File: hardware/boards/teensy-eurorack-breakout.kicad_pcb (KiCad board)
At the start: 4 copper layers, 110.5 x 111.1 mm, 76 parts, among them J1 Conn_01x08, SW1 Rotary_Encoder_Switch, SW2 Rotary_Encoder_Switch, SW3 Rotary_Encoder_Switch, U2 AD5754BREZ, U3 AD5754BREZ, U5 MCP1700-2502E, U6 AD7606BSTZ, U7 6N138

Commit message: schematic, pcb changes for v2.0
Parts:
- removed R2: 4.7k, Resistor_SMD:R_0805_2012Metric
- C19, C21, C23, C25, C31, C32, C33, C34: footprint Capacitor_SMD:C_0805_2012Metric -> Capacitors_THT:CP_Radial_D5.0mm_P2.00mm
- moved C19 41.8 mm to (105.4, 113.7), turned to 0 degrees
- moved C23 40.3 mm to (105.4, 107.3), turned to 0 degrees
- moved C32 40.2 mm to (99.1, 107.3), turned to 0 degrees
- moved U5 35.8 mm to (126.9, 123.3)
- moved C33 33.5 mm to (99.1, 113.7), turned to 0 degrees
- moved C30 31.2 mm to (120.0, 102.9)
- moved C27 30.7 mm to (126.9, 131.2), turned to 0 degrees
- moved C28 30.7 mm to (126.9, 127.5), turned to 0 degrees
- moved U3 29.7 mm to (118.1, 96.5), turned to 270 degrees
- moved C29 25.9 mm to (115.9, 102.9), turned to 180 degrees
- moved C37 25.3 mm to (109.5, 102.9), turned to 0 degrees
- moved C39 24.5 mm to (105.7, 102.9)
- moved C34 20.5 mm to (120.0, 113.7), turned to 0 degrees
- moved C35 17.0 mm to (142.2, 114.9), turned to 270 degrees
- moved C31 16.6 mm to (120.0, 107.3), turned to 0 degrees
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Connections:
- JB1 pad 13: +12V -> -12V
- JB1 pad 14: -12V -> +12V
- JB1 pad 5: Net-(JB1-Pad5) -> GND
- JB1 pad 6: Net-(JB1-Pad6) -> /ADC_RESET
- JB1 pad 7: Net-(JB1-Pad7) -> GND
- JB2 pad 13: +12V -> (no net)
- JB2 pad 14: -12V -> (no net)
- JB2 pad 3: /ADC_SCK -> /ADC_RANGE
- JB2 pad 7: /DAC_SDOUT -> GND
- JOUT1 pad TN: Net-(JOUT1-PadTN) -> (no net)
- JOUT2 pad TN: Net-(JOUT2-PadTN) -> (no net)
- JOUT3 pad TN: Net-(JOUT3-PadTN) -> (no net)
- JOUT4 pad TN: Net-(JOUT4-PadTN) -> (no net)
- JOUT5 pad TN: Net-(JOUT5-PadTN) -> (no net)
- JOUT6 pad TN: Net-(JOUT6-PadTN) -> (no net)
- JOUT7 pad TN: Net-(JOUT7-PadTN) -> (no net)
- JOUT8 pad TN: Net-(JOUT8-PadTN) -> (no net)
- MIDI_IN1 pad 1: Net-(MIDI_IN1-Pad1) -> (no net)
- MIDI_IN1 pad 3: Net-(MIDI_IN1-Pad3) -> (no net)
- MIDI_IN1 pad 5: Net-(MIDI_IN1-Pad5) -> (no net)
- MIDI_OUT1 pad 1: Net-(MIDI_OUT1-Pad1) -> (no net)
- MIDI_OUT1 pad 3: Net-(MIDI_OUT1-Pad3) -> (no net)
- MIDI_OUT1 pad 5: Net-(MIDI_OUT1-Pad5) -> (no net)
- R1 pad 2: Net-(R1-Pad2) -> /ADC_RESET
- U2 pad 12: Net-(U2-Pad12) -> (no net)
- U2 pad 13: Net-(U2-Pad13) -> (no net)
- U2 pad 2: Net-(U2-Pad2) -> (no net)
- U2 pad 6: Net-(U2-Pad6) -> (no net)
- U3 pad 12: Net-(U3-Pad12) -> (no net)
- U3 pad 13: Net-(U3-Pad13) -> (no net)
- U3 pad 16: /DAC_SDOUT -> (no net)
- U3 pad 2: Net-(U3-Pad2) -> (no net)
- U3 pad 6: Net-(U3-Pad6) -> (no net)
- U6 pad 11: Net-(R1-Pad2) -> /ADC_RESET
- U6 pad 12: /ADC_SCK -> /DAC_SCK
- U6 pad 15: Net-(U6-Pad15) -> (no net)
- U6 pad 42: Net-(U6-Pad42) -> (no net)
- U6 pad 8: Net-(R2-Pad1) -> /ADC_RANGE
- U7 pad 1: Net-(U7-Pad1) -> (no net)
- U7 pad 4: Net-(U7-Pad4) -> (no net)
- U7 pad 7: Net-(U7-Pad7) -> (no net)
- USBA1 pad 5: Net-(USBA1-Pad5) -> (no net)
- USBA1 pad 6: Net-(USBA1-Pad6) -> (no net)
- USBB1 pad 5: Net-(USBB1-Pad5) -> (no net)
- USBB1 pad 6: Net-(USBB1-Pad6) -> (no net)
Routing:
- net GND: track 97.8 -> 817.8 mm, vias 22 -> 239
- net /VOUT5: track 42.6 -> 197.7 mm
- net +5V: track 198.0 -> 315.4 mm, vias 0 -> 5
- net /ADC_RESET: track 0.00 -> 75.3 mm
- net /VOUT7: track 46.6 -> 115.2 mm
- net +12V: track 129.5 -> 61.5 mm, vias 2 -> 1
- net /DAC_SDOUT: track 59.7 -> 0.00 mm, vias 1 -> 0
- net /ADC_RANGE: track 0.00 -> 57.1 mm
- net /ADC_SCK: track 56.7 -> 0.00 mm, vias 1 -> 0
- net /VOUT8: track 51.3 -> 105.1 mm, vias 1 -> 0
- net +3V3: track 391.8 -> 442.4 mm, vias 0 -> 9
- net Net-(D1-Pad2): track 47.3 -> 94.5 mm, vias 1 -> 0
- net /DAC_SCK: track 59.8 -> 106.9 mm, vias 2 -> 3
- net /DAC_SDIN: track 20.6 -> 67.2 mm, vias 1 -> 0
- net -12V: track 138.4 -> 91.9 mm, vias 1 -> 3
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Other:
- copper layers 4 -> 2

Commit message: corrections to breakout pcb
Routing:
- net GND: track 817.8 -> 83.6 mm, vias 239 -> 242
- net /DAC_REF2V5: track 121.8 -> 68.4 mm, vias 0 -> 2
- net /DAC_SDIN: track 67.2 -> 19.4 mm, vias 0 -> 2
- net Net-(U2-Pad16): track 23.4 -> 25.0 mm, vias 4 -> 2

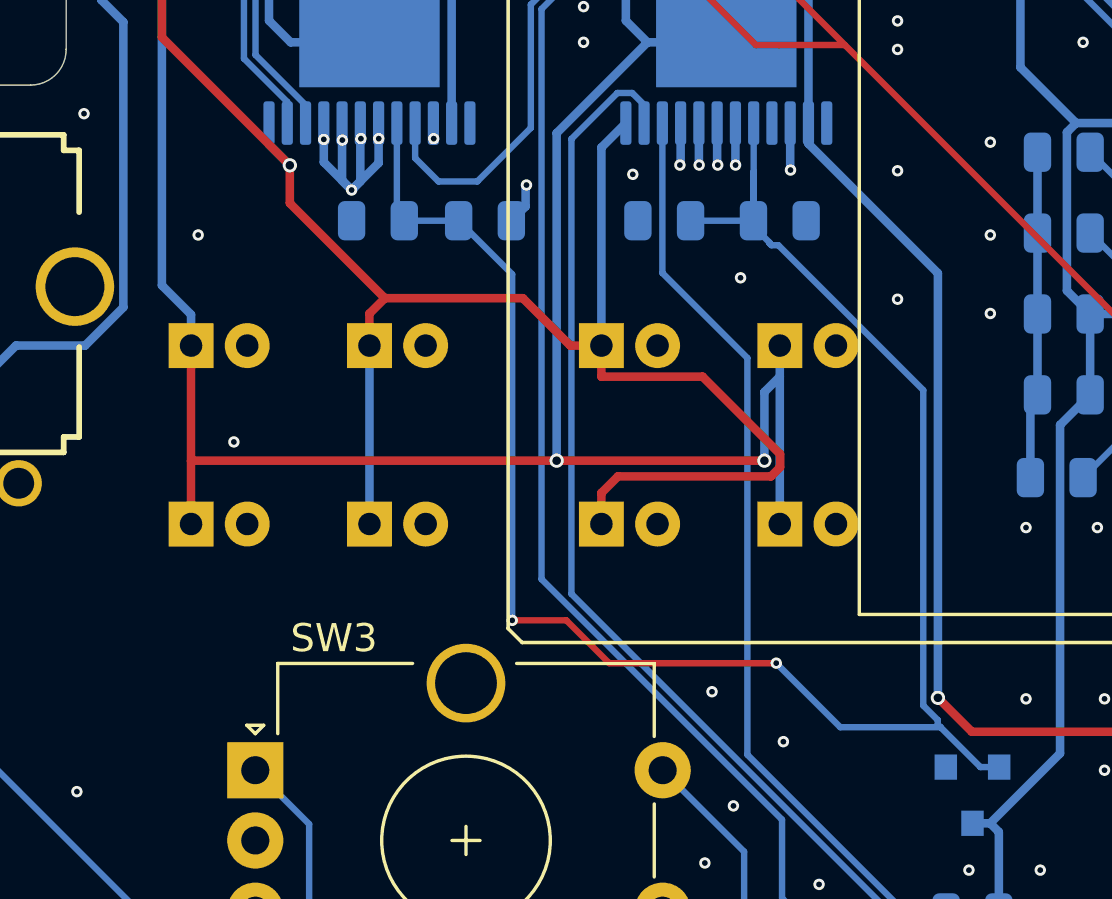
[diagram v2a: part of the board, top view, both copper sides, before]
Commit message: pcb: update polatity of +-12v bypass caps
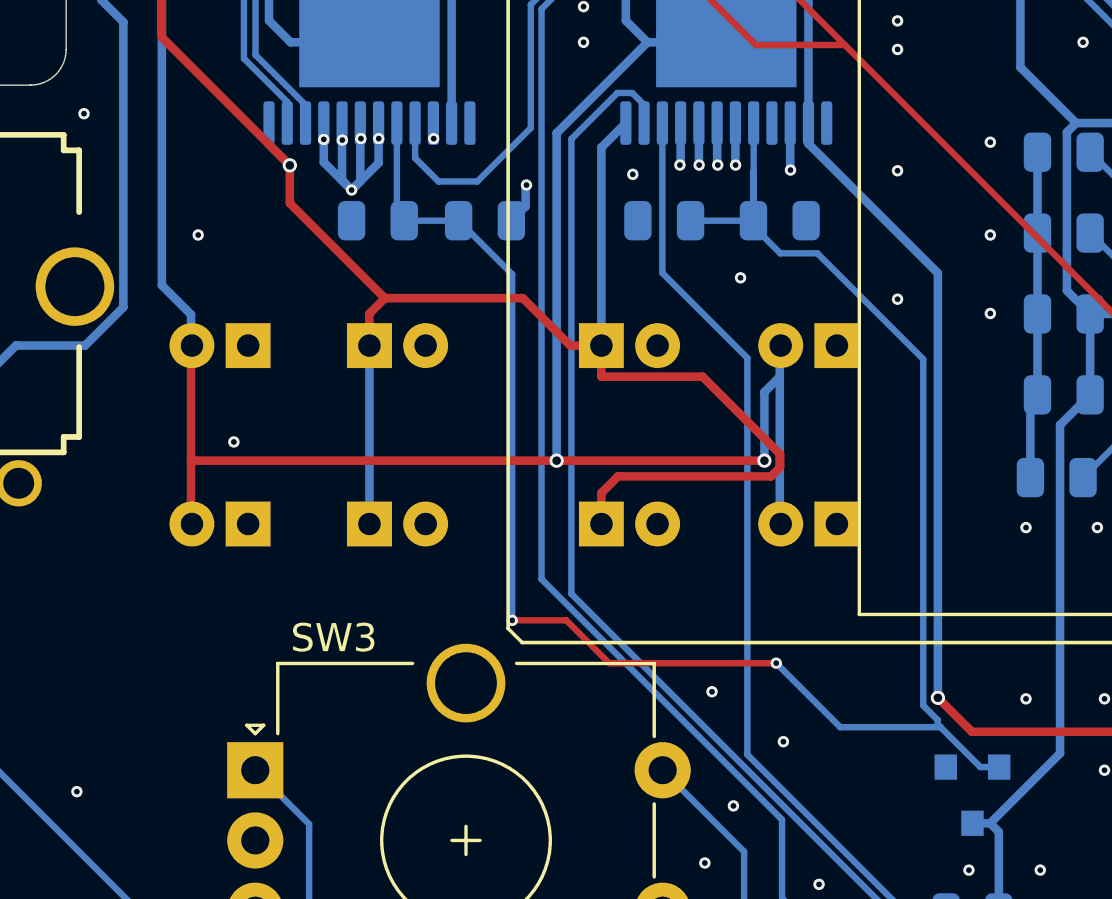
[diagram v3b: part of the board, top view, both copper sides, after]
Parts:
- moved C31 2.03 mm to (122.0, 107.3), turned to 180 degrees
- moved C32 2.03 mm to (101.1, 107.3), turned to 180 degrees
- moved C33 2.03 mm to (101.1, 113.7), turned to 180 degrees
- moved C34 2.03 mm to (122.0, 113.7), turned to 180 degrees
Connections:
- C31 pad 1: -12V -> GND
- C31 pad 2: GND -> -12V
- C32 pad 1: -12V -> GND
- C32 pad 2: GND -> -12V
- C33 pad 1: -12V -> GND
- C33 pad 2: GND -> -12V
- C34 pad 1: -12V -> GND
- C34 pad 2: GND -> -12V
- JB2 pad 13: (no net) -> Net-(JB2-Pad13)
- JB2 pad 14: (no net) -> Net-(JB2-Pad14)
- JOUT1 pad TN: (no net) -> Net-(JOUT1-PadTN)
- JOUT2 pad TN: (no net) -> Net-(JOUT2-PadTN)
- JOUT3 pad TN: (no net) -> Net-(JOUT3-PadTN)
- JOUT4 pad TN: (no net) -> Net-(JOUT4-PadTN)
- JOUT5 pad TN: (no net) -> Net-(JOUT5-PadTN)
- JOUT6 pad TN: (no net) -> Net-(JOUT6-PadTN)
- JOUT7 pad TN: (no net) -> Net-(JOUT7-PadTN)
- JOUT8 pad TN: (no net) -> Net-(JOUT8-PadTN)
- MIDI_IN1 pad 1: (no net) -> Net-(MIDI_IN1-Pad1)
- MIDI_IN1 pad 3: (no net) -> Net-(MIDI_IN1-Pad3)
- MIDI_IN1 pad 5: (no net) -> Net-(MIDI_IN1-Pad5)
- MIDI_OUT1 pad 1: (no net) -> Net-(MIDI_OUT1-Pad1)
- MIDI_OUT1 pad 3: (no net) -> Net-(MIDI_OUT1-Pad3)
- MIDI_OUT1 pad 5: (no net) -> Net-(MIDI_OUT1-Pad5)
- U2 pad 12: (no net) -> Net-(U2-Pad12)
- U2 pad 13: (no net) -> Net-(U2-Pad13)
- U2 pad 2: (no net) -> Net-(U2-Pad2)
- U2 pad 6: (no net) -> Net-(U2-Pad6)
- U3 pad 12: (no net) -> Net-(U3-Pad12)
- U3 pad 13: (no net) -> Net-(U3-Pad13)
- U3 pad 16: (no net) -> Net-(U3-Pad16)
- U3 pad 2: (no net) -> Net-(U3-Pad2)
- U3 pad 6: (no net) -> Net-(U3-Pad6)
- U6 pad 15: (no net) -> Net-(U6-Pad15)
- U6 pad 42: (no net) -> Net-(U6-Pad42)
- U7 pad 1: (no net) -> Net-(U7-Pad1)
- U7 pad 4: (no net) -> Net-(U7-Pad4)
- U7 pad 7: (no net) -> Net-(U7-Pad7)
- USBA1 pad 5: (no net) -> Net-(USBA1-Pad5)
- USBA1 pad 6: (no net) -> Net-(USBA1-Pad6)
- USBB1 pad 5: (no net) -> Net-(USBB1-Pad5)
- USBB1 pad 6: (no net) -> Net-(USBB1-Pad6)
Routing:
- net /DAC_REF2V5: track 68.4 -> 69.0 mm

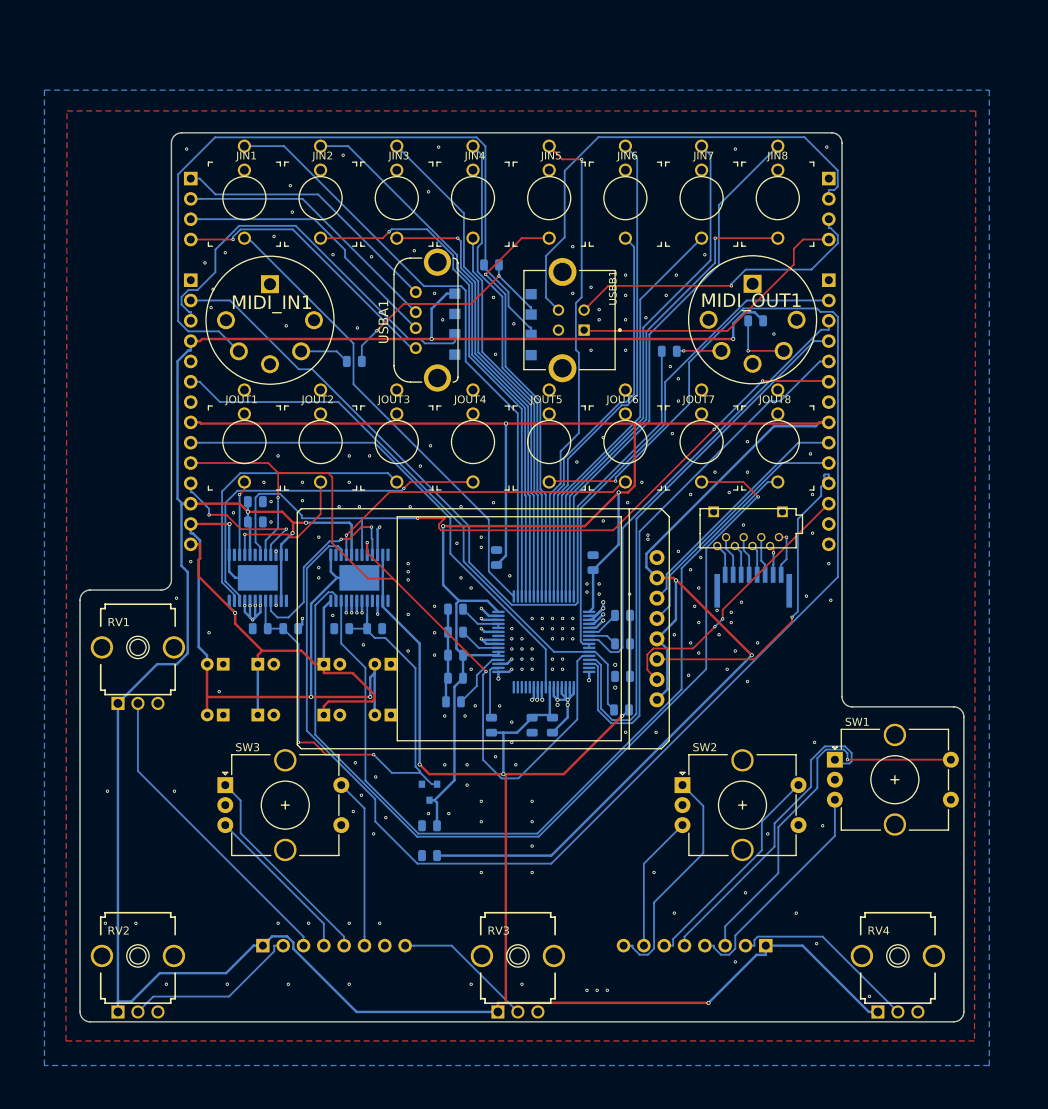
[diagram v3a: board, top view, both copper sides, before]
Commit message: pcb: update from schematic and route as 4 layer board
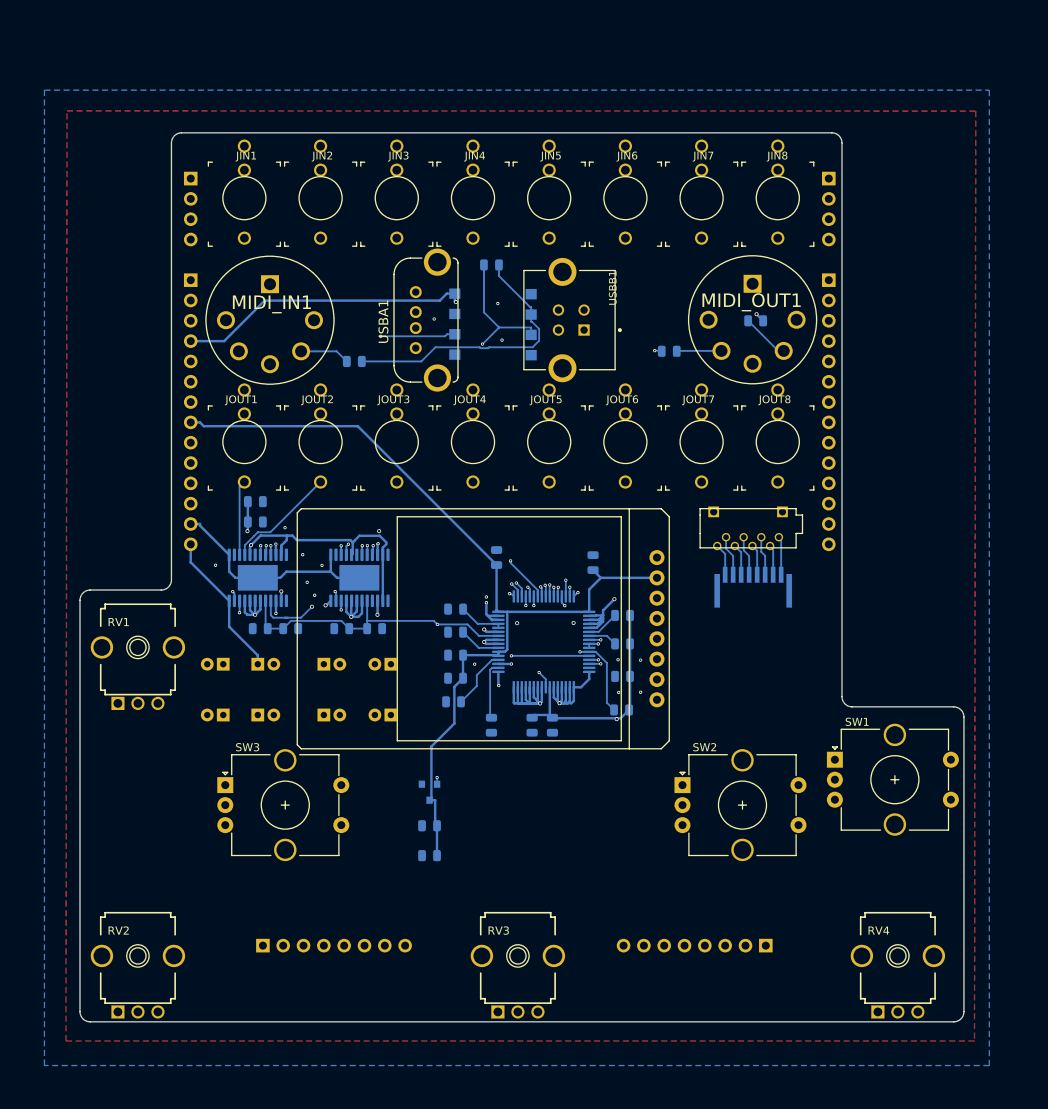
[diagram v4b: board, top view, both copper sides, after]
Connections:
- R7 pad 1: +3V3 -> GND
- U6 pad 42: Net-(U6-Pad42) -> /DAC_REF2V5
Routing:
- net /VOUT5: track 197.7 -> 31.6 mm
- net +5V: track 315.4 -> 161.1 mm, vias 5 -> 0
- net /VOUT7: track 115.2 -> 52.7 mm
- net +3V3: track 442.4 -> 383.0 mm, vias 9 -> 6
- net Net-(D1-Pad2): track 94.5 -> 48.5 mm, vias 0 -> 1
- net /DAC_SCK: track 106.9 -> 64.0 mm
- net /VOUT8: track 105.1 -> 62.3 mm, vias 0 -> 1
- net /MIDI_TX: track 102.7 -> 63.2 mm, vias 0 -> 2
- net Net-(JBUSBB1-Pad2): track 61.0 -> 39.5 mm
- net /ADC_CS: track 70.2 -> 53.3 mm, vias 0 -> 1
- net /ADC_BUSY: track 68.4 -> 51.7 mm, vias 0 -> 1
- net /MIDI_RX: track 50.2 -> 33.9 mm, vias 0 -> 1
- net GND: track 83.6 -> 99.6 mm, vias 242 -> 31
- net /DAC_SYNC: track 96.2 -> 82.7 mm, vias 3 -> 2
- net +12V: track 61.5 -> 48.0 mm
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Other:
- copper layers 2 -> 4

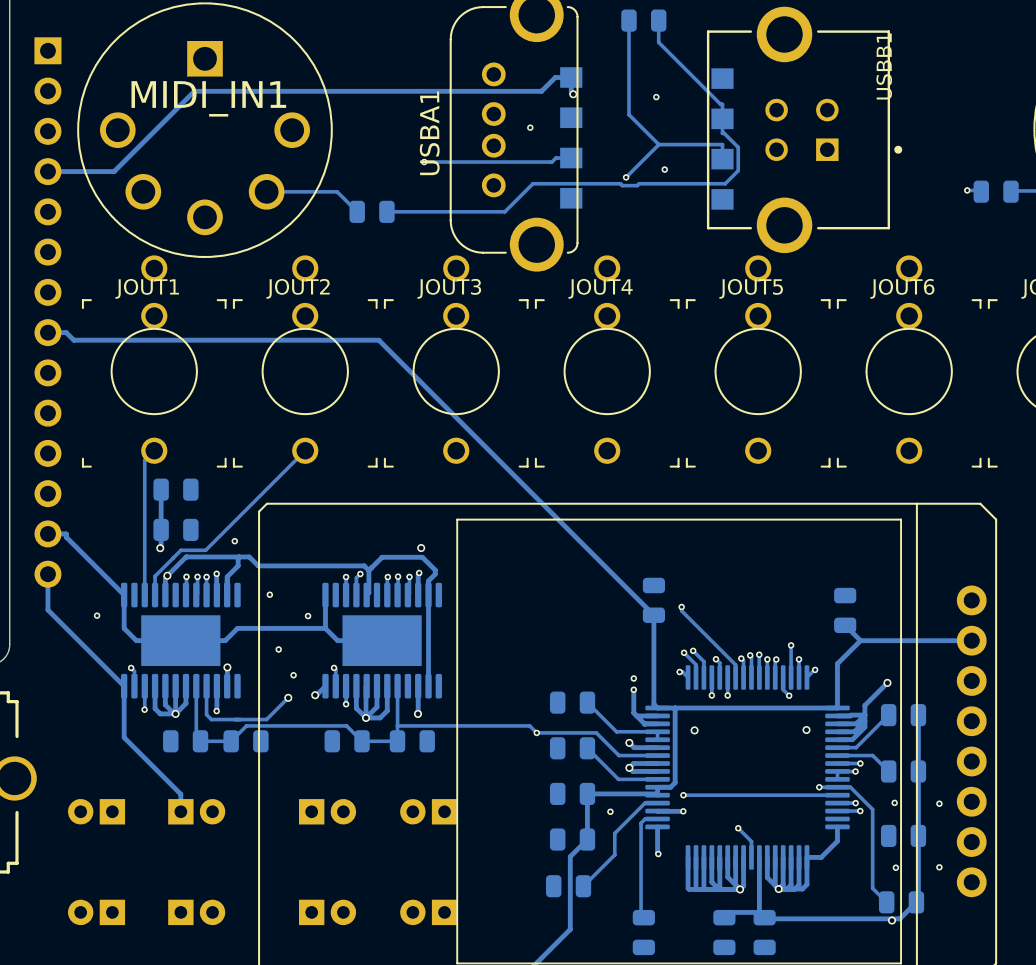
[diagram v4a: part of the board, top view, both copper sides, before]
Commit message: pcb: increase diameter of some via from 0.2mm to 0.25mm for jlcpcb
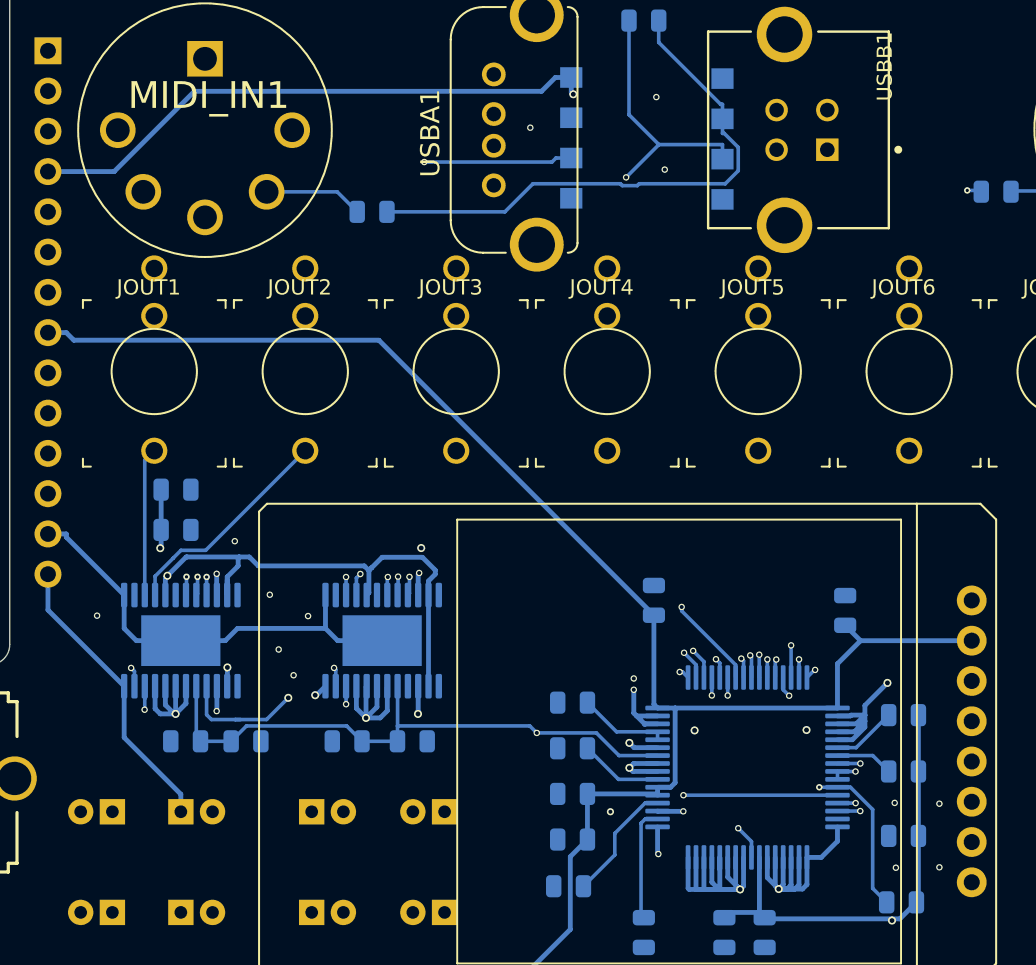
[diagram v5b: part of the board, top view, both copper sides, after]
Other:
- net class Default: via_dia 0.4064 -> 0.4; via_drill 0.2032 -> 0.25
- rule via_min_drill: 0.1016 -> 0.25
- rule via_min_size: 0.2032 -> 0.4
